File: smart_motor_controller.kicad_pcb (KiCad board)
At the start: 4 copper layers, 75 x 60 mm, 79 parts, among them J10 USB_B_Micro, J101 Conn_02x07_Odd_Even, J102 I2C_CONN, J104 Debug, J301 M0_CONN, J302 M1_CONN, J303 M2_CONN, J304 M3_CONN, J309 External encoders power, J310 Encoder Commector, J9 Input 12V, SW102 SW_NRST, SW103 SW_NRST, U2 STM32F405RGT6, U201 TPS54331DDAR, U3 USBLC6-2SC6, U301 DRV8870DDA, U302 DRV8870DDA, U303 DRV8870DDA, U304 DRV8870DDA

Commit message: Initial changes
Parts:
- removed D301: B5819W, Diode_SMD:D_SOD-123
- removed J10: USB_B_Micro, VsReality_Footprints:U-F-M5DD-W-L
- removed J302: M1_CONN, VsReality_Footprints:Ningbo_Kangnex_Elec_WJ128V_5_0_2P
- removed J303: M2_CONN, VsReality_Footprints:Ningbo_Kangnex_Elec_WJ128V_5_0_2P
- removed J304: M3_CONN, VsReality_Footprints:Ningbo_Kangnex_Elec_WJ128V_5_0_2P
- removed J309: External encoders power, Connector_PinHeader_2.54mm:PinHeader_1x02_P2.54mm_Vertical
- removed J310: Encoder Commector, VsReality_Footprints:Encoder_PinHeader_4x04_P2.54mm_Vertical
- removed R103, R104: 15, Resistor_SMD:R_0603_1608Metric
- removed R304: 0.15, Resistor_SMD:R_0603_1608Metric
- removed U302, U303, U304: DRV8870DDA, Package_SO:Texas_HTSOP-8-1EP_3.9x4.9mm_P1.27mm_EP2.95x4.9mm_Mask2.4x3.1mm_ThermalVias
- added C1: 100nf, Capacitor_SMD:C_0603_1608Metric, F.Cu at (166.5, 73.1)
- added C10: 10uf, Capacitor_SMD:C_1206_3216Metric, F.Cu at (105.7, 76.1)
- added C11: 10uf, Capacitor_SMD:C_1206_3216Metric, F.Cu at (114.2, 76.1)
- added C12: 10uf, Capacitor_SMD:C_1206_3216Metric, F.Cu at (107.8, 63.6)
- added C2: 100nf, Capacitor_SMD:C_0603_1608Metric, F.Cu at (165.5, 77.8)
- added C302: 100n, Capacitor_SMD:C_0603_1608Metric, F.Cu at (146.5, 141.3)
- added C304: 1u, Capacitor_SMD:C_0603_1608Metric, F.Cu at (147.4, 131.7)
- added C305: 47n, Capacitor_SMD:C_0603_1608Metric, F.Cu at (145.8, 139.0)
- added C306: 1u, Capacitor_SMD:C_0603_1608Metric, F.Cu at (144.2, 140.5)
- added C311: 100n, Capacitor_SMD:C_0603_1608Metric, F.Cu at (152.9, 136.0)
- added C314: 1u, Capacitor_SMD:C_0603_1608Metric, F.Cu at (163.2, 131.7)
- added C315: 47n, Capacitor_SMD:C_0603_1608Metric, F.Cu at (161.5, 139.0)
- added C316: 1u, Capacitor_SMD:C_0603_1608Metric, F.Cu at (160.0, 140.5)
- added C321: 100n, Capacitor_SMD:C_0603_1608Metric, F.Cu at (178.0, 141.3)
- added C324: 1u, Capacitor_SMD:C_0603_1608Metric, F.Cu at (179.0, 131.7)
- added C325: 47n, Capacitor_SMD:C_0603_1608Metric, F.Cu at (177.2, 139.1)
- added C326: 1u, Capacitor_SMD:C_0603_1608Metric, F.Cu at (175.8, 140.6)
- added C331: 100n, Capacitor_SMD:C_0603_1608Metric, F.Cu at (194.0, 141.3)
- added C334: 1u, Capacitor_SMD:C_0603_1608Metric, F.Cu at (194.6, 131.7)
- added C335: 47n, Capacitor_SMD:C_0603_1608Metric, F.Cu at (193.3, 139.1)
- added C336: 1u, Capacitor_SMD:C_0603_1608Metric, F.Cu at (191.5, 140.6)
- added C601: 100nf, Capacitor_SMD:C_0603_1608Metric, F.Cu at (198.3, 65.0)
- added C602: 100nf, Capacitor_SMD:C_0603_1608Metric, F.Cu at (200.5, 72.8)
- added C9: 100nf, Capacitor_SMD:C_0603_1608Metric, F.Cu at (165.5, 80.3)
- added D401: B5819W, Diode_SMD:D_SOD-123, F.Cu at (195.7, 88.5)
- added J311: M0_CONN, VsReality_Footprints:Ningbo_Kangnex_Elec_WJ128V_5_0_2P, F.Cu at (159.5, 150.1)
- added J321: M0_CONN, VsReality_Footprints:Ningbo_Kangnex_Elec_WJ128V_5_0_2P, F.Cu at (169.5, 150.1)
- added J331: M0_CONN, VsReality_Footprints:Ningbo_Kangnex_Elec_WJ128V_5_0_2P, F.Cu at (179.5, 150.1)
- added J401: Encoder Commector, VsReality_Footprints:Encoder_PinHeader_4x04_P2.54mm_Vertical, F.Cu at (193.5, 77.2)
- added J402: External encoders power, Connector_PinHeader_2.54mm:PinHeader_1x02_P2.54mm_Vertical, F.Cu at (201.0, 89.5)
- added J501: USB_C_Receptacle_USB2.0_16P, Connector_USB:USB_C_Receptacle_GCT_USB4105-xx-A_16P_TopMnt_Horizontal, F.Cu at (127.6, 69.0)
- added PT3.3V1: TestPoint_Small, TestPoint:TestPoint_Pad_D1.5mm, F.Cu at (113.2, 59.4)
- added R311: 10K, Resistor_SMD:R_0603_1608Metric, F.Cu at (161.8, 128.6)
- added R312: 330, Resistor_SMD:R_0603_1608Metric, F.Cu at (154.2, 127.8)
- added R313: 330, Resistor_SMD:R_0603_1608Metric, F.Cu at (152.2, 130.9)
- added R321: 10K, Resistor_SMD:R_0603_1608Metric, F.Cu at (177.7, 128.6)
- added R322: 330, Resistor_SMD:R_0603_1608Metric, F.Cu at (172.2, 128.6)
- added R323: 330, Resistor_SMD:R_0603_1608Metric, F.Cu at (168.8, 128.6)
- added R331: 10K, Resistor_SMD:R_0603_1608Metric, F.Cu at (193.4, 129.1)
- added R332: 330, Resistor_SMD:R_0603_1608Metric, F.Cu at (188.5, 128.6)
- added R333: 330, Resistor_SMD:R_0603_1608Metric, F.Cu at (185.0, 128.6)
- added R501: 5.1k, Resistor_SMD:R_0603_1608Metric, F.Cu at (134.4, 66.5)
- added R502: 5.1k, Resistor_SMD:R_0603_1608Metric, F.Cu at (134.4, 71.5)
- added R503: 15, Resistor_SMD:R_0603_1608Metric, F.Cu at (145.6, 68.0)
- added R504: 15, Resistor_SMD:R_0603_1608Metric, F.Cu at (145.6, 70.0)
- added TP3.3V_Backup1: TestPoint_Small, TestPoint:TestPoint_Pad_D1.5mm, F.Cu at (114.2, 72.1)
- added U1: STM32F405VGTx, Package_QFP:LQFP-100_14x14mm_P0.5mm, F.Cu at (176.5, 75.5)
- added U202: AP2112K-3.3, Package_TO_SOT_SMD:SOT-23-5, F.Cu at (109.9, 75.5)
- added U311: DRV8873S, VsReality_Footprints:HTSSOP-24_L7.8-W4.4-P0.65-LS6.4-TL-EP, F.Cu at (158.0, 134.0)
- added U321: DRV8873S, VsReality_Footprints:HTSSOP-24_L7.8-W4.4-P0.65-LS6.4-TL-EP, F.Cu at (173.8, 134.1)
- added U331: DRV8873S, VsReality_Footprints:HTSSOP-24_L7.8-W4.4-P0.65-LS6.4-TL-EP, F.Cu at (189.5, 134.1)
- added U501: USBLC6-2SC6, Package_TO_SOT_SMD:SOT-23-6, F.Cu at (141.5, 69.0)
- C14: value 10n -> 10nf
- J104: value Debug -> SWD; footprint Connector_PinHeader_2.54mm:PinHeader_1x04_P2.54mm_Vertical -> Connector_PinHeader_1.27mm:PinHeader_2x05_P1.27mm_Vertical
- R301: value 0.15 -> 10K
- R302, R303: value 0.15 -> 330
- U2: value STM32F405RGT6 -> BMI088; footprint Package_QFP:LQFP-64_10x10mm_P0.5mm -> Package_LGA:Bosch_LGA-16_4.5x3mm_P0.5mm_LayoutBorder7x1y_ClockwisePinNumbering
- U3: value USBLC6-2SC6 -> TPS2116DRL; footprint Package_TO_SOT_SMD:SOT-23-6 -> Package_TO_SOT_SMD:SOT-583-8
- U301: value DRV8870DDA -> DRV8873S; footprint Package_SO:Texas_HTSOP-8-1EP_3.9x4.9mm_P1.27mm_EP2.95x4.9mm_Mask2.4x3.1mm_ThermalVias -> VsReality_Footprints:HTSSOP-24_L7.8-W4.4-P0.65-LS6.4-TL-EP
- moved C101 54.8 mm to (202.6, 98.2), turned to -90 degrees
- moved SW103 54.7 mm to (200.0, 99.5), turned to 90 degrees
- moved R302 48.2 mm to (140.7, 128.5), turned to 0 degrees
- moved C312 46.3 mm to (162.3, 141.3), turned to -90 degrees
- moved C333 45.7 mm to (198.0, 142.3), turned to 90 degrees
- moved C323 44.9 mm to (181.8, 142.3), turned to 90 degrees
- moved C313 44.4 mm to (166.0, 142.3), turned to 90 degrees
- moved C303 44.2 mm to (150.2, 142.3), turned to 90 degrees
- moved C301 43.1 mm to (137.4, 136.0)
- moved C322 41.5 mm to (168.8, 136.0), turned to -90 degrees
- moved C332 41.2 mm to (184.5, 136.1), turned to -90 degrees
- moved R303 40.9 mm to (137.2, 128.5), turned to 180 degrees
- moved U301 40.7 mm to (142.2, 134.0)
- moved J301 40.4 mm to (149.5, 150.1), turned to 180 degrees
- moved U2 31.0 mm to (200.0, 68.8)
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- renumbered C302 to C303, C303 to C312, C304 to C313, C305 to C322, C306 to C323, C307 to C332, C308 to C333, 3.3V201 to TP3.3VMainIn1
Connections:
- C15 pad 1: Net-(U2-VCAP_1) -> Net-(U1-VCAP_1)
- C16 pad 1: Net-(U2-VCAP_2) -> Net-(U1-VCAP_2)
- C206 pad 1: +3V3 -> 3.3V_MainIn
- C207 pad 1: +3V3 -> 3.3V_MainIn
- J104 pad 1: GND -> +3V3
- J104 pad 2: SWCLK -> SWDIO
- J104 pad 3: SWDIO -> GND
- J104 pad 4: NRST -> SWCLK
- L201 pad 2: +3V3 -> 3.3V_MainIn
- R201 pad 1: +3V3 -> 3.3V_MainIn
- R301 pad 1: Net-(U301-ISEN) -> +3V3
- R301 pad 2: GND -> M0_nFAULT
- R302 pad 1: Net-(U302-ISEN) -> M0_IPROPI1
- R303 pad 1: Net-(U303-ISEN) -> M0_IPROPI2
- TP3.3VMainIn1 pad 1: +3V3 -> 3.3V_MainIn
- U2 pad 1: +3V3 -> IMU_INT2_ACCEL
- U2 pad 10: unconnected-(U2-PC2-Pad10) -> IMU_MISO
- U2 pad 11: unconnected-(U2-PC3-Pad11) -> +3V3
- U2 pad 12: GND -> IMU_INT3_GYRO
- U2 pad 13: +3.3VA -> IMU_INT4_GYRO
- U2 pad 14: ENCODER_1_A -> IMU_CSB1_ACCEL
- U2 pad 15: ENCODER_1_B -> IMU_MISO
- U2 pad 16: LED -> IMU_INT1_ACCEL
- U2 pad 2: unconnected-(U2-PC13-Pad2) -> GND
- U2 pad 3: unconnected-(U2-PC14-Pad3) -> +3V3
- U2 pad 4: unconnected-(U2-PC15-Pad4) -> GND
- U2 pad 5: HSE_IN -> IMU_CSB1_GYRO
- U2 pad 6: HSE_OUT -> GND
- U2 pad 7: NRST -> GND
- U2 pad 8: unconnected-(U2-PC0-Pad8) -> IMU_SCK
- U2 pad 9: unconnected-(U2-PC1-Pad9) -> IMU_SDI
- U3 pad 1: USB_CONN_D- -> GND
- U3 pad 2: GND -> +3V3
- U3 pad 3: USB_CONN_D+ -> 3.3V_MainIn
- U3 pad 4: Net-(R104-Pad2) -> 3.3V_MainIn
- U3 pad 5: +5V -> 3.3V_MainIn
- U3 pad 6: Net-(R103-Pad1) -> 3.3V_USB
- U301 pad 1: GND -> Net-(U301-DVDD)
- U301 pad 2: M0_OUT2 -> M0_nFAULT
- U301 pad 3: M0_OUT1 -> M_SDO
- U301 pad 4: +3V3 -> M_SDI
- U301 pad 5: VMOTORS -> M_SCLK
- U301 pad 6: Net-(J301-Pin_1) -> M0_nSCS
- U301 pad 7: Net-(U301-ISEN) -> M0_EN
- U301 pad 8: Net-(J301-Pin_2) -> M0_PH
- U301 pad 9: GND -> M0_DISABLE
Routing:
- net VMOTORS: track 124.1 -> 7.79 mm, vias 0 -> 55
- net NRST: track 58.4 -> 6.35 mm
- net M_SDO: track 0.00 -> 51.6 mm, vias 0 -> 2
- net SWDIO: track 47.2 -> 0.00 mm, vias 1 -> 0
- net SWCLK: track 43.7 -> 0.00 mm, vias 1 -> 0
- net USB_D-: track 37.6 -> 0.00 mm, vias 2 -> 0
- net USB_D+: track 37.4 -> 0.00 mm, vias 2 -> 0
- net CAN2_TX: track 35.7 -> 0.00 mm, vias 1 -> 0
- net M0_OUT2: track 34.4 -> 0.00 mm, vias 2 -> 0
- net M0_OUT1: track 34.0 -> 0.00 mm, vias 2 -> 0
- net CAN2_RX: track 33.6 -> 0.00 mm, vias 1 -> 0
- net BOOT0: track 36.2 -> 2.80 mm, vias 2 -> 0
- net M3_OUT2: track 32.8 -> 0.00 mm
- net M3_OUT1: track 31.7 -> 0.00 mm
- net ENCODER_1_B: track 30.4 -> 0.00 mm, vias 1 -> 0
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- removed copper zone on F.Cu, net Net-(J301-Pin_1)
- removed copper zone on F.Cu, net Net-(J301-Pin_2)
- removed copper zone on F.Cu, net Net-(J302-Pin_1)
- removed copper zone on F.Cu, net Net-(J302-Pin_2)
- removed copper zone on F.Cu, net Net-(J303-Pin_1)
- removed copper zone on F.Cu, net Net-(J303-Pin_2)
- removed copper zone on F.Cu, net Net-(J304-Pin_1)
- removed copper zone on F.Cu, net Net-(J304-Pin_2)
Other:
- board size 75 x 60 mm -> 81 x 66 mm
- board text removed: "0"
- board text removed: "3"
- board text removed: "A"
- board text removed: "B"
- board text removed: "CLK"
- board text removed: "ENCODERS"
- board text removed: "IO"
- board text removed: "USB"
- board text removed: "VUSB"

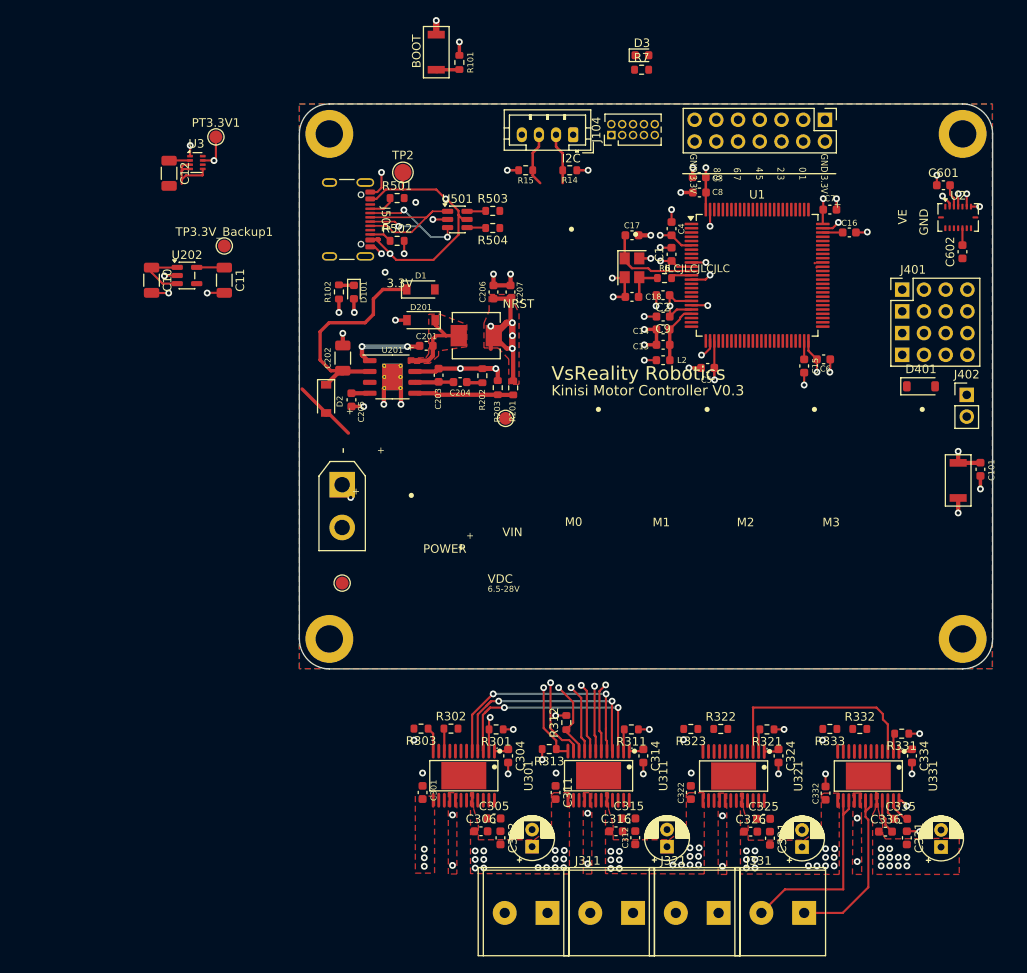
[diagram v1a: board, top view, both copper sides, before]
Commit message: Add USB sensing and power management components to the schematic
- Introduced a junction for USB sensing at coordinates (173.99, 64.77).
- Added multiple wires connecting various components to the new junction.
- Created a global label "USB_SENSE" for the USB sensing functionality.
- Updated references for power components to a new numbering scheme (#PWR0501 to #PWR0509).
- Added resistors R505 and R506 with specified values and footprints.
- Included power symbols for +5V and GND with appropriate references and properties.
- Ensured all new components are included in the BOM and marked for simulation.
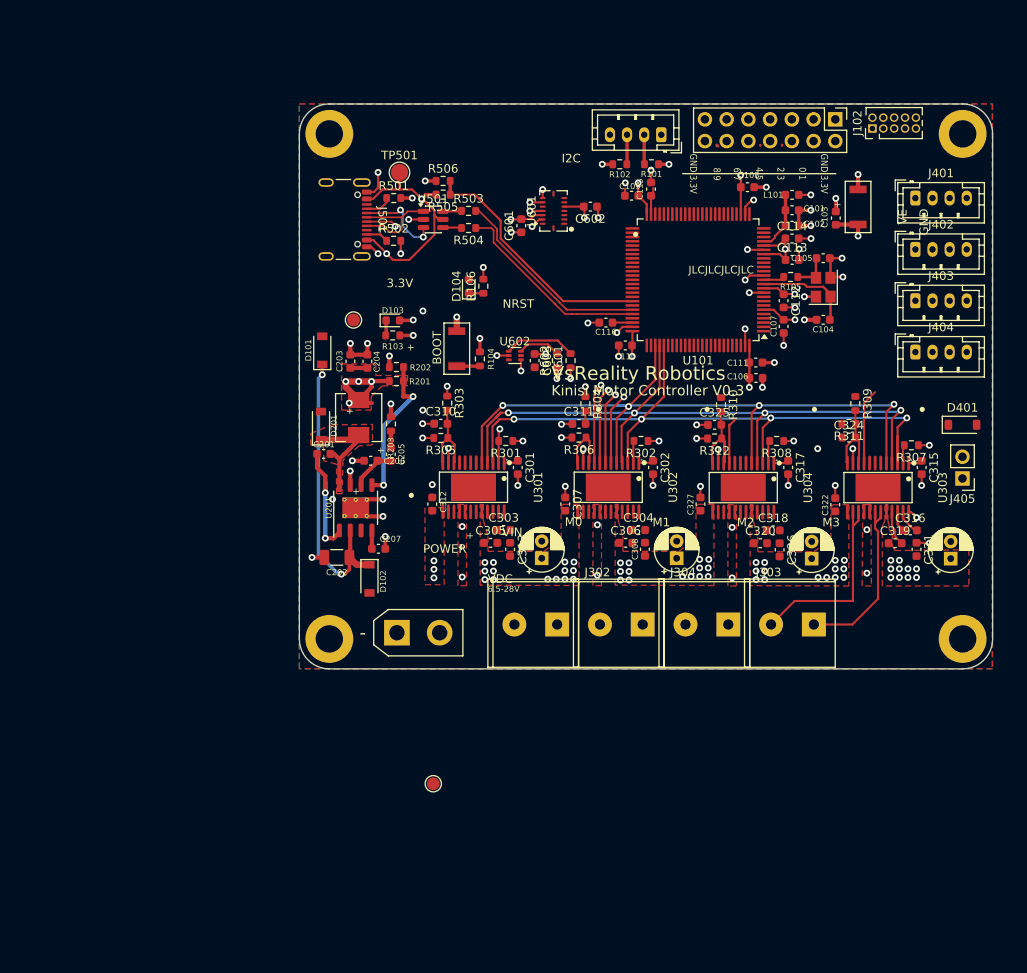
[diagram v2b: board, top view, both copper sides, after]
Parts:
- removed C10, C11, C12: 10uf, Capacitor_SMD:C_1206_3216Metric
- removed PT3.3V1, TP3.3V_Backup1: TestPoint_Small, TestPoint:TestPoint_Pad_D1.5mm
- removed U202: AP2112K-3.3, Package_TO_SOT_SMD:SOT-23-5
- removed U3: TPS2116DRL, Package_TO_SOT_SMD:SOT-583-8
- added C310: 1u, Capacitor_SMD:C_0603_1608Metric, F.Cu at (139.5, 92.9)
- added C311: 1u, Capacitor_SMD:C_0603_1608Metric, F.Cu at (155.7, 92.9)
- added C324: 1u, Capacitor_SMD:C_0603_1608Metric, F.Cu at (187.2, 94.5)
- added C325: 1u, Capacitor_SMD:C_0603_1608Metric, F.Cu at (171.5, 93.0)
- added C603: 10nf, Capacitor_SMD:C_0603_1608Metric, F.Cu at (150.5, 85.5)
- added J402: Encoder Connector 1, Connector_JST:JST_PH_B4B-PH-K_1x04_P2.00mm_Vertical, F.Cu at (195.0, 72.5)
- added J403: Encoder Connector 2, Connector_JST:JST_PH_B4B-PH-K_1x04_P2.00mm_Vertical, F.Cu at (195.0, 78.5)
- added J404: Encoder Connector 3, Connector_JST:JST_PH_B4B-PH-K_1x04_P2.00mm_Vertical, F.Cu at (195.0, 84.5)
- added R505: 4K7, Resistor_SMD:R_0603_1608Metric, F.Cu at (139.8, 66.1)
- added R506: 10K, Resistor_SMD:R_0603_1608Metric, F.Cu at (139.8, 64.5)
- added R601: 4k7, Resistor_SMD:R_0603_1608Metric, F.Cu at (154.7, 85.5)
- added R602: 4k7, Resistor_SMD:R_0603_1608Metric, F.Cu at (153.1, 85.5)
- added U602: TMP102xxDRL, Package_TO_SOT_SMD:SOT-563, F.Cu at (148.2, 84.9)
- J401: value Encoder Commector -> Encoder Connector 0; footprint VsReality_Footprints:Encoder_PinHeader_4x04_P2.54mm_Vertical -> Connector_JST:JST_PH_B4B-PH-K_1x04_P2.00mm_Vertical
- R303: value 330 -> 100
- R304: renamed from R313; value 330 -> 100
- R309: renamed from R333; value 330 -> 100
- R310: renamed from R323; value 330 -> 100
- moved C601 49.6 mm to (148.9, 69.7), turned to 90 degrees
- moved U601 47.3 mm to (152.7, 68.0), turned to 90 degrees
- moved C602 43.8 mm to (157.0, 67.5), turned to 180 degrees
- moved R304 40.6 mm to (156.4, 90.5), turned to -90 degrees
- moved R303 38.2 mm to (140.3, 90.5), turned to -90 degrees
- moved R309 38.2 mm to (188.0, 90.5), turned to -90 degrees
- moved R310 38.1 mm to (172.3, 90.7), turned to -90 degrees
- moved R311 35.7 mm to (187.2, 92.9), turned to 180 degrees
- moved R104 34.7 mm to (144.1, 85.3)
- moved SW102 34.7 mm to (141.4, 84.1)
- moved SW101 34.0 mm to (188.3, 67.5), turned to -90 degrees
- moved R305 34.0 mm to (139.5, 94.5), turned to 180 degrees
- moved R312 34.0 mm to (171.5, 94.6), turned to 180 degrees
- moved C103 33.9 mm to (185.7, 68.8), turned to 90 degrees
- moved D104 33.7 mm to (142.8, 76.8), turned to 90 degrees
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- renumbered C13 to C101, C14 to C102, C101 to C103, C17 to C104, C18 to C105, C3 to C106, C4 to C107, C5 to C108, C6 to C109, C7 to C110, C8 to C111, C1 to C112, C2 to C113, C9 to C114, C15 to C115, C16 to C116, C206 to C203, C207 to C204, C204 to C205, C203 to C206, C205 to C207, C304 to C301, C314 to C302, C305 to C303, C315 to C304, C306 to C305, C316 to C306, C311 to C307, C312 to C308, C313 to C309, C301 to C312, C302 to C313, C303 to C314, C334 to C315, C335 to C316, C324 to C317, C325 to C318, C336 to C319, C326 to C320, C331 to C321, C332 to C322, C333 to C323, C321 to C326, C322 to C327, C323 to C328, D1 to D101, D2 to D102, D101 to D103, D3 to D104, HSE1 to HSE101, J102 to J101, J104 to J102, J9 to J103, J101 to J104, J311 to J302, J331 to J303, J321 to J304, J402 to J405, L2 to L101, R14 to R101, R15 to R102, R102 to R103, R101 to R104, R6 to R105, R7 to R106, R203 to R202, R202 to R203, R311 to R302, R302 to R305, R312 to R306, R331 to R307, R321 to R308, R332 to R311, R322 to R312, SW103 to SW101, TP1 to TP101, TP3.3VMainIn1 to TP3.3V201, TP2 to TP501, U1 to U101, U311 to U302, U331 to U303, U321 to U304, U2 to U601
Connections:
- C203 pad 1: 3.3V_MainIn -> +3V3
- C204 pad 1: 3.3V_MainIn -> +3V3
- J401 pad 3: ENCODER_0_B -> ENCODER_0_A
- J401 pad 4: ENCODER_0_A -> ENCODER_0_B
- L201 pad 2: 3.3V_MainIn -> +3V3
- R201 pad 1: 3.3V_MainIn -> +3V3
- R303 pad 1: M0_IPROPI2 -> M0_IPROPI
- R303 pad 2: GND -> Net-(U301-IPROPI1)
- R304 pad 1: M1_IPROPI2 -> M1_IPROPI
- R304 pad 2: GND -> Net-(U302-IPROPI1)
- R305 pad 1: M0_IPROPI1 -> Net-(U301-IPROPI1)
- R306 pad 1: M1_IPROPI1 -> Net-(U302-IPROPI1)
- R309 pad 1: M3_IPROPI2 -> M3_IPROPI
- R309 pad 2: GND -> Net-(U303-IPROPI1)
- R310 pad 1: M2_IPROPI2 -> M2_IPROPI
- R310 pad 2: GND -> Net-(U304-IPROPI1)
- R311 pad 1: M3_IPROPI1 -> Net-(U303-IPROPI1)
- R312 pad 1: M2_IPROPI1 -> Net-(U304-IPROPI1)
- TP3.3V201 pad 1: 3.3V_MainIn -> +3V3
- U101 pad 17: unconnected-(U1-PC2-Pad17) -> IMU_MISO
- U101 pad 18: unconnected-(U1-PC3-Pad18) -> IMU_SDI
- U101 pad 39: unconnected-(U1-PE8-Pad39) -> M0_EN
- U101 pad 41: unconnected-(U1-PE10-Pad41) -> M1_EN
- U101 pad 43: unconnected-(U1-PE12-Pad43) -> M2_EN
- U101 pad 46: unconnected-(U1-PE15-Pad46) -> M3_EN
- U101 pad 47: I2C2_SCL -> IMU_SCK
- U101 pad 48: I2C2_SDA -> unconnected-(U101-PB11-Pad48)
- U101 pad 51: CAN2_RX -> unconnected-(U101-PB12-Pad51)
- U101 pad 52: CAN2_TX -> unconnected-(U101-PB13-Pad52)
- U101 pad 53: M0_OUT1 -> unconnected-(U101-PB14-Pad53)
- U101 pad 54: M0_OUT2 -> unconnected-(U101-PB15-Pad54)
- U101 pad 63: M2_OUT1 -> ENCODER_3_A
- U101 pad 64: M2_OUT2 -> ENCODER_3_B
- U101 pad 65: M1_OUT1 -> unconnected-(U101-PC8-Pad65)
- U101 pad 66: M1_OUT2 -> SENSOR_SDA
- U101 pad 67: M3_OUT1 -> SENSOR_SCL
- U101 pad 68: M3_OUT2 -> USB_SENSE
- U101 pad 77: ENCODER_3_A -> unconnected-(U101-PA15-Pad77)
- U101 pad 78: USART3_TX -> M_SCLK
- U101 pad 79: USART3_RX -> M_SDI
- U101 pad 80: GPIO3 -> M_SDO
- U101 pad 83: GPIO2 -> unconnected-(U101-PD2-Pad83)
- U101 pad 89: ENCODER_3_B -> SWO
- U101 pad 90: GPIO1 -> unconnected-(U101-PB4-Pad90)
- U101 pad 91: GPIO0 -> unconnected-(U101-PB5-Pad91)
- U101 pad 95: I2C1_SCL -> unconnected-(U101-PB8-Pad95)
- U101 pad 96: I2C1_SDA -> unconnected-(U101-PB9-Pad96)
- U301 pad 10: M0_IPROPI1 -> Net-(U301-IPROPI1)
- U301 pad 12: M0_IPROPI2 -> Net-(U301-IPROPI1)
- U302 pad 10: M1_IPROPI1 -> Net-(U302-IPROPI1)
- U302 pad 12: M1_IPROPI2 -> Net-(U302-IPROPI1)
- U303 pad 10: M3_IPROPI1 -> Net-(U303-IPROPI1)
- U303 pad 12: M3_IPROPI2 -> Net-(U303-IPROPI1)
- U304 pad 10: M2_IPROPI1 -> Net-(U304-IPROPI1)
- U304 pad 12: M2_IPROPI2 -> Net-(U304-IPROPI1)
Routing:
- net M_SCLK: track 27.6 -> 84.9 mm, vias 2 -> 4
- net M_SDI: track 27.3 -> 82.7 mm, vias 2 -> 4
- net M_SDO: track 51.6 -> 83.9 mm, vias 2 -> 4
- net USB_SENSE: track 0.00 -> 29.3 mm
- net 3.3V_MainIn: track 27.3 -> 0.00 mm, vias 4 -> 0
- net USB_D-: track 0.00 -> 24.1 mm
- net USB_D+: track 0.00 -> 23.3 mm
- net +3V3: track 57.2 -> 73.9 mm, vias 17 -> 25
- net Net-(U304-IPROPI1): track 0.00 -> 12.5 mm
- net +5V: track 37.8 -> 27.4 mm
- net M1_IPROPI2: track 10.0 -> 0.00 mm, vias 1 -> 0
- net Net-(U303-IPROPI1): track 0.00 -> 9.86 mm
- net Net-(U301-IPROPI1): track 0.00 -> 9.73 mm
- net Net-(U302-IPROPI1): track 0.00 -> 9.61 mm
- net M1_IPROPI1: track 9.31 -> 0.00 mm, vias 1 -> 0
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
